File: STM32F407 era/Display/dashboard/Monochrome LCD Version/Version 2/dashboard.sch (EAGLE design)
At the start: 89 parts, among them IC2 74HC14D, IC3 74HC14D, U1 CAT4238TD-GT3

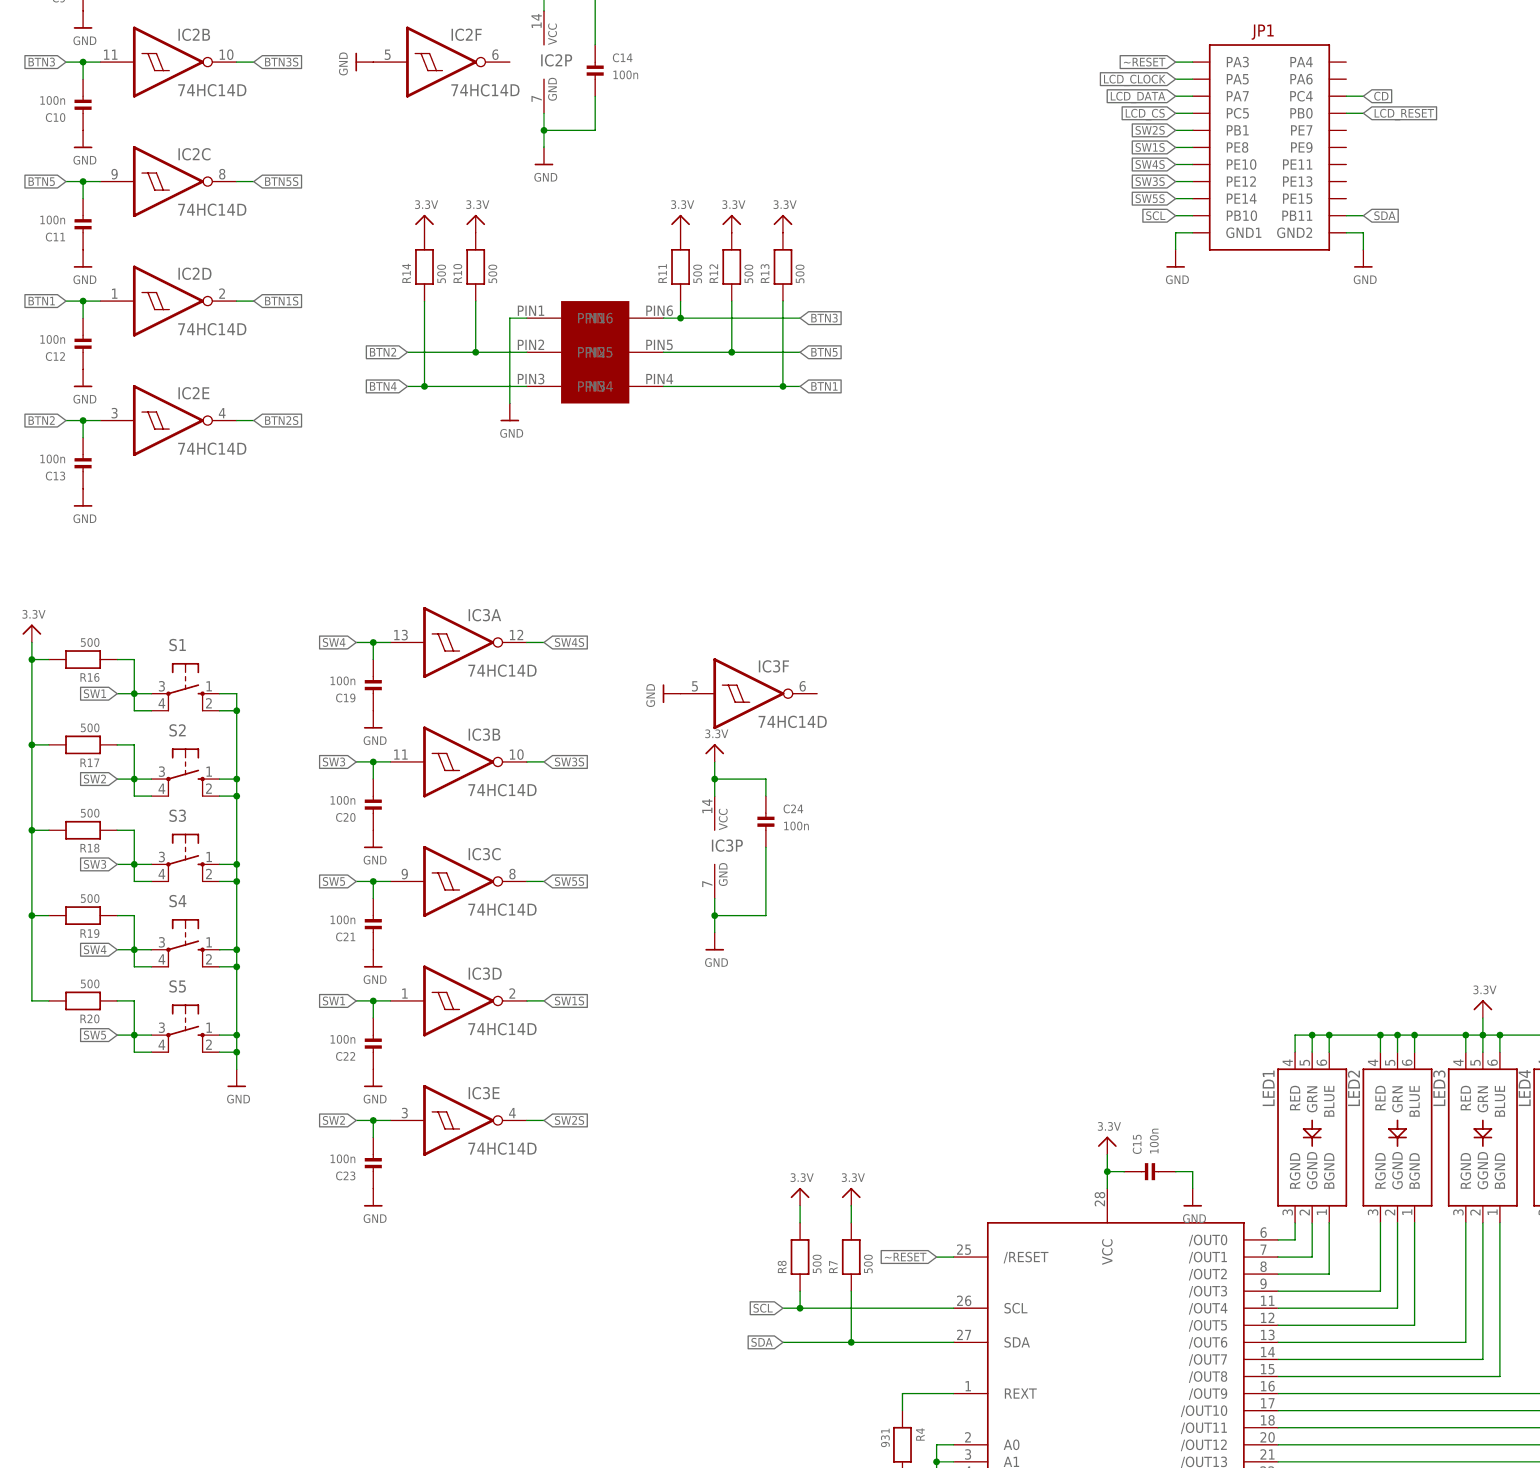
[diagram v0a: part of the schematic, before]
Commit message: fixed silkscreen and added extra button for interface
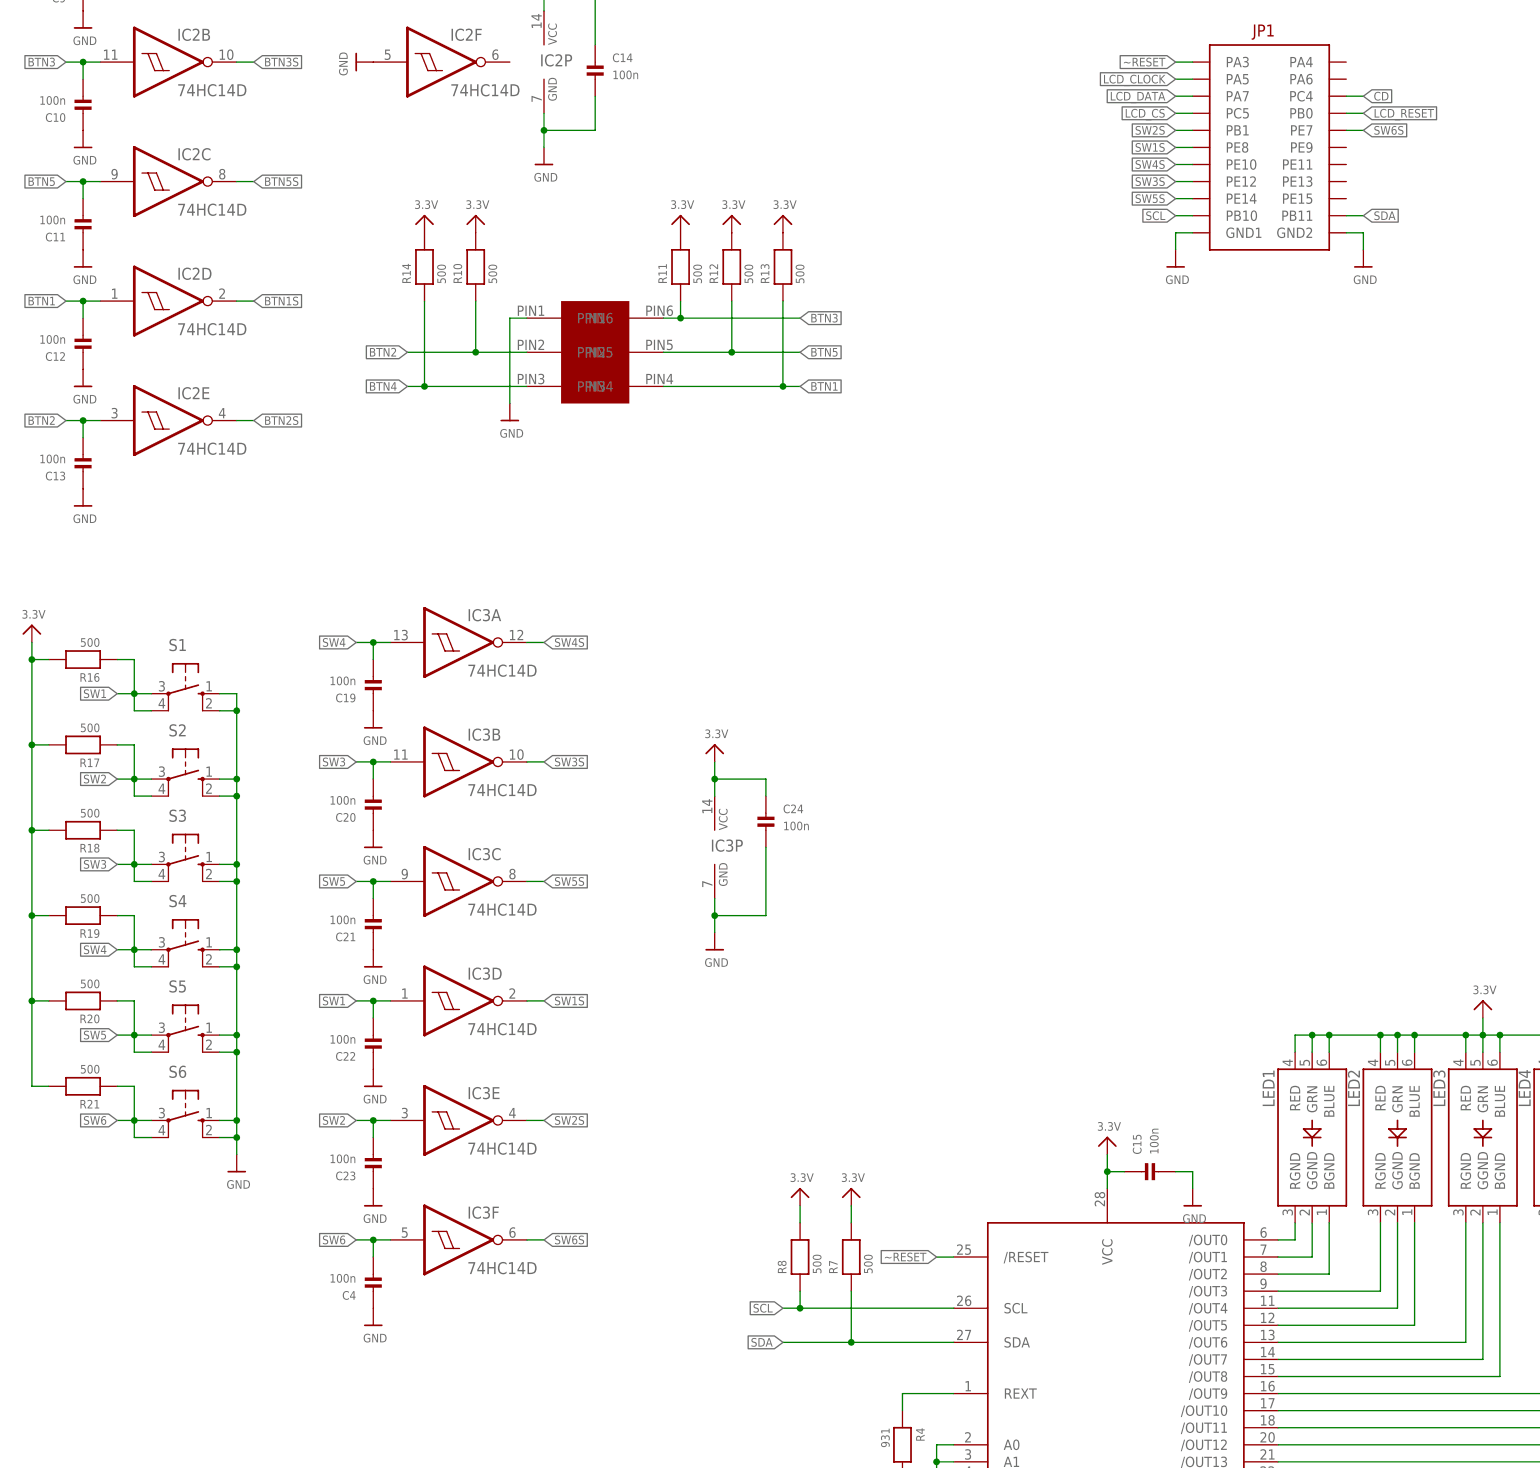
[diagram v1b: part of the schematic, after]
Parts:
- added C4: 100n, microbuilder:CAP_CERAMIC_0603
- added R21: 500, microbuilder:RESISTOR_0603
- added S6: (no value), switch-omron:10-XX
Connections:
- new net SW6: C4.P$2, IC3F.I, R21.1, S6.P, S6.P1
- new net SW6S: IC3F.O, U$1G$1.PE7
- net 3.3V: now also R21.2
- net GND: now also C4.P$1, S6.S, S6.S1; no longer IC3F.I
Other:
- moved on the sheet: IC3F
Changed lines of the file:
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@@
 <part name="U$71" library="microbuilder" deviceset="GND" device=""/>
 <part name="C24" library="microbuilder" deviceset="CAP_CERAMIC" device="_0603" value="100n"/>
-<part name="U$72" library="microbuilder" deviceset="GND" device=""/>
 <part name="U$73" library="microbuilder" deviceset="GND" device=""/>
 <part name="U$74" library="microbuilder" deviceset="3.3V" device=""/>
@@
 <part name="C25" library="rcl" deviceset="CPOL-EU" device="153CLV-1012" value="470u"/>
 <part name="C26" library="rcl" deviceset="CPOL-EU" device="153CLV-1012" value="220u"/>
+<part name="S6" library="switch-omron" deviceset="10-XX" device="">
+<attribute name="MF" value=""/>
+<attribute name="MPN" value="B3F-1000"/>
+<attribute name="OC_FARNELL" value="176432"/>
+<attribute name="OC_NEWARK" value="36M3542"/>
+</part>
+<part name="R21" library="microbuilder" deviceset="RESISTOR" device="_0603" value="500"/>
+<part name="C4" library="microbuilder" deviceset="CAP_CERAMIC" device="_0603" value="100n"/>
+<part name="U$72" library="microbuilder" deviceset="GND" device=""/>
 </parts>
 <sheets>
@@
 <instance part="S3" gate="1" x="-210.82" y="-55.88" rot="R270"/>
 <instance part="S4" gate="1" x="-210.82" y="-68.58" rot="R270"/>
-<instance part="U$53" gate="G$1" x="-203.2" y="-88.9"/>
+<instance part="U$53" gate="G$1" x="-203.2" y="-101.6"/>
 <instance part="R16" gate="G$1" x="-226.06" y="-25.4" rot="R180"/>
 <instance part="R17" gate="G$1" x="-226.06" y="-38.1" rot="R180"/>
@@
 <instance part="U$70" gate="G$1" x="-182.88" y="-88.9"/>
 <instance part="U$71" gate="G$1" x="-182.88" y="-106.68"/>
-<instance part="IC3" gate="F" x="-127" y="-30.48"/>
+<instance part="IC3" gate="F" x="-170.18" y="-111.76"/>
 <instance part="IC3" gate="P" x="-132.08" y="-53.34"/>
 <instance part="C24" gate="G$1" x="-124.46" y="-50.8"/>
-<instance part="U$72" gate="G$1" x="-139.7" y="-30.48" rot="R270"/>
 <instance part="U$73" gate="G$1" x="-132.08" y="-68.58"/>
 <instance part="U$74" gate="G$1" x="-132.08" y="-38.1"/>
@@
 <instance part="C25" gate="G$1" x="25.4" y="-53.34" rot="MR0"/>
 <instance part="C26" gate="G$1" x="83.82" y="-53.34" rot="MR0"/>
+<instance part="S6" gate="1" x="-210.82" y="-93.98" rot="R270"/>
+<instance part="R21" gate="G$1" x="-226.06" y="-88.9" rot="R180"/>
+<instance part="C4" gate="G$1" x="-182.88" y="-116.84" rot="R180"/>
+<instance part="U$72" gate="G$1" x="-182.88" y="-124.46"/>
 </instances>
 <busses>
@@
 <pinref part="S4" gate="1" pin="S"/>
 <wire x1="-203.2" y1="-81.28" x2="-203.2" y2="-83.82" width="0.1524" layer="91"/>
-<wire x1="-203.2" y1="-83.82" x2="-203.2" y2="-86.36" width="0.1524" layer="91"/>
+<wire x1="-203.2" y1="-83.82" x2="-203.2" y2="-93.98" width="0.1524" layer="91"/>
+<wire x1="-203.2" y1="-93.98" x2="-203.2" y2="-96.52" width="0.1524" layer="91"/>
+<wire x1="-203.2" y1="-96.52" x2="-203.2" y2="-99.06" width="0.1524" layer="91"/>
 <wire x1="-205.74" y1="-68.58" x2="-203.2" y2="-68.58" width="0.1524" layer="91"/>
 <wire x1="-203.2" y1="-68.58" x2="-203.2" y2="-71.12" width="0.1524" layer="91"/>
@@
 <wire x1="-205.74" y1="-81.28" x2="-203.2" y2="-81.28" width="0.1524" layer="91"/>
 <junction x="-203.2" y="-81.28"/>
+<pinref part="S6" gate="1" pin="S"/>
+<wire x1="-205.74" y1="-93.98" x2="-203.2" y2="-93.98" width="0.1524" layer="91"/>
+<junction x="-203.2" y="-93.98"/>
+<pinref part="S6" gate="1" pin="S1"/>
+<wire x1="-205.74" y1="-96.52" x2="-203.2" y2="-96.52" width="0.1524" layer="91"/>
+<junction x="-203.2" y="-96.52"/>
 </segment>
 <segment>
@@
 <pinref part="C23" gate="G$1" pin="P$1"/>
 <pinref part="U$71" gate="G$1" pin="GND"/>
-</segment>
-<segment>
-<pinref part="IC3" gate="F" pin="I"/>
-<pinref part="U$72" gate="G$1" pin="GND"/>
 </segment>
 <segment>
@@
 <wire x1="83.82" y1="-58.42" x2="83.82" y2="-63.5" width="0.1524" layer="91"/>
 <pinref part="C26" gate="G$1" pin="-"/>
+</segment>
+<segment>
+<pinref part="C4" gate="G$1" pin="P$1"/>
+<pinref part="U$72" gate="G$1" pin="GND"/>
 </segment>
 </net>
@@
 <wire x1="-233.68" y1="-76.2" x2="-233.68" y2="-63.5" width="0.1524" layer="91"/>
 <junction x="-233.68" y="-63.5"/>
+<pinref part="R21" gate="G$1" pin="2"/>
+<wire x1="-231.14" y1="-88.9" x2="-233.68" y2="-88.9" width="0.1524" layer="91"/>
+<wire x1="-233.68" y1="-88.9" x2="-233.68" y2="-76.2" width="0.1524" layer="91"/>
+<junction x="-233.68" y="-76.2"/>
 </segment>
 <segment>
@@
 </segment>
 </net>
+<net name="SW6" class="0">
+<segment>
+<pinref part="S6" gate="1" pin="P"/>
+<wire x1="-215.9" y1="-93.98" x2="-218.44" y2="-93.98" width="0.1524" layer="91"/>
+<wire x1="-218.44" y1="-93.98" x2="-218.44" y2="-88.9" width="0.1524" layer="91"/>
+<pinref part="R21" gate="G$1" pin="1"/>
+<wire x1="-218.44" y1="-88.9" x2="-220.98" y2="-88.9" width="0.1524" layer="91"/>
+<pinref part="S6" gate="1" pin="P1"/>
+<wire x1="-215.9" y1="-96.52" x2="-218.44" y2="-96.52" width="0.1524" layer="91"/>
+<wire x1="-218.44" y1="-96.52" x2="-218.44" y2="-93.98" width="0.1524" layer="91"/>
+<junction x="-218.44" y="-93.98"/>
+<wire x1="-220.98" y1="-93.98" x2="-218.44" y2="-93.98" width="0.1524" layer="91"/>
+<label x="-220.98" y="-93.98" size="1.27" layer="95" rot="R180" xref="yes"/>
+</segment>
+<segment>
+<pinref part="C4" gate="G$1" pin="P$2"/>
+<wire x1="-182.88" y1="-111.76" x2="-182.88" y2="-114.3" width="0.1524" layer="91"/>
+<wire x1="-185.42" y1="-111.76" x2="-182.88" y2="-111.76" width="0.1524" layer="91"/>
+<pinref part="IC3" gate="F" pin="I"/>
+<wire x1="-182.88" y1="-111.76" x2="-180.34" y2="-111.76" width="0.1524" layer="91"/>
+<junction x="-182.88" y="-111.76"/>
+<label x="-185.42" y="-111.76" size="1.27" layer="95" rot="R180" xref="yes"/>
+</segment>
+</net>
+<net name="SW6S" class="0">
+<segment>
+<pinref part="IC3" gate="F" pin="O"/>
+<wire x1="-157.48" y1="-111.76" x2="-160.02" y2="-111.76" width="0.1524" layer="91"/>
+<label x="-157.48" y="-111.76" size="1.27" layer="95" xref="yes"/>
+</segment>
+<segment>
+<pinref part="U$1" gate="G$1" pin="PE7"/>
+<wire x1="-35.56" y1="53.34" x2="-38.1" y2="53.34" width="0.1524" layer="91"/>
+<label x="-35.56" y="53.34" size="1.27" layer="95" xref="yes"/>
+</segment>
+</net>

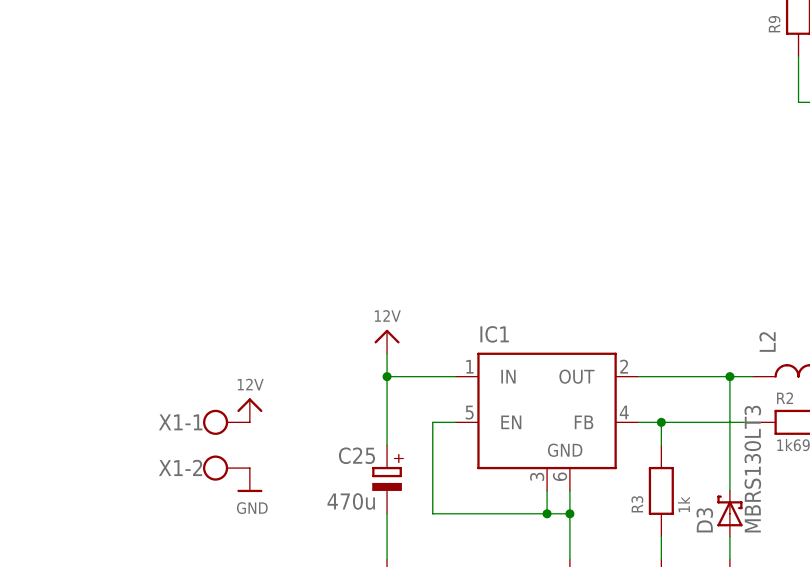
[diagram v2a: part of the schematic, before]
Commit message: adding last changes to accomendate changes in H-Bridge
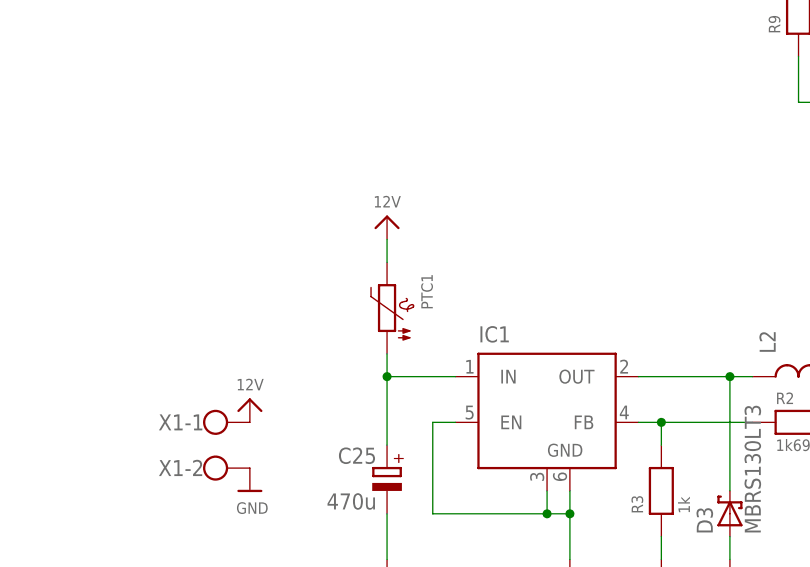
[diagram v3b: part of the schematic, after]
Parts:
- added PTC1: (no value), microbuilder:PTC1812
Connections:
- new net N$77: C25.+, IC1.IN, PTC1.1
- net 12V: now also PTC1.2; no longer C25.+, IC1.IN
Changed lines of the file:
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@@
 <part name="C4" library="microbuilder" deviceset="CAP_CERAMIC" device="_0603" value="100n"/>
 <part name="U$72" library="microbuilder" deviceset="GND" device=""/>
+<part name="PTC1" library="microbuilder" deviceset="PTC" device="1812"/>
 </parts>
 <sheets>
@@
 <instance part="R3" gate="G$1" x="55.88" y="-55.88" rot="R90"/>
 <instance part="U$19" gate="G$1" x="55.88" y="-66.04"/>
-<instance part="U$20" gate="G$1" x="25.4" y="-38.1"/>
+<instance part="U$20" gate="G$1" x="25.4" y="-25.4"/>
 <instance part="U$21" gate="G$1" x="25.4" y="-66.04"/>
 <instance part="U$22" gate="G$1" x="83.82" y="-66.04"/>
@@
 <instance part="C4" gate="G$1" x="-182.88" y="-116.84" rot="R180"/>
 <instance part="U$72" gate="G$1" x="-182.88" y="-124.46"/>
+<instance part="PTC1" gate="G$1" x="25.4" y="-35.56" rot="R270"/>
 </instances>
 <busses>
@@
 </segment>
 <segment>
-<pinref part="IC1" gate="G$1" pin="IN"/>
+<pinref part="PTC1" gate="G$1" pin="2"/>
 <pinref part="U$20" gate="G$1" pin="12V"/>
-<wire x1="33.02" y1="-43.18" x2="25.4" y2="-43.18" width="0.1524" layer="91"/>
-<wire x1="25.4" y1="-43.18" x2="25.4" y2="-40.64" width="0.1524" layer="91"/>
-<wire x1="25.4" y1="-43.18" x2="25.4" y2="-50.8" width="0.1524" layer="91"/>
-<junction x="25.4" y="-43.18"/>
-<pinref part="C25" gate="G$1" pin="+"/>
+<wire x1="25.4" y1="-30.48" x2="25.4" y2="-27.94" width="0.1524" layer="91"/>
 </segment>
 </net>
@@
 </segment>
 </net>
+<net name="N$77" class="0">
+<segment>
+<pinref part="IC1" gate="G$1" pin="IN"/>
+<wire x1="33.02" y1="-43.18" x2="25.4" y2="-43.18" width="0.1524" layer="91"/>
+<wire x1="25.4" y1="-43.18" x2="25.4" y2="-50.8" width="0.1524" layer="91"/>
+<pinref part="C25" gate="G$1" pin="+"/>
+<pinref part="PTC1" gate="G$1" pin="1"/>
+<wire x1="25.4" y1="-40.64" x2="25.4" y2="-43.18" width="0.1524" layer="91"/>
+<junction x="25.4" y="-43.18"/>
+</segment>
+</net>

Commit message: created Gerbers
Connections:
- net BTN1S: now also U$1G$2.PB13; no longer U$1G$2.PB12
- net BTN2S: now also U$1G$2.PB15; no longer U$1G$2.PB13
- net BTN3S: now also U$1G$2.PD11; no longer U$1G$2.PB14
- net BTN4S: now also U$1G$2.PC6; no longer U$1G$2.PD9
- net BTN5S: now also U$1G$2.PD9; no longer U$1G$2.PB15
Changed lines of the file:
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@@
 <net name="BTN1S" class="0">
-<segment>
-<pinref part="U$1" gate="G$2" pin="PB12"/>
-<wire x1="0" y1="63.5" x2="5.08" y2="63.5" width="0.1524" layer="91"/>
-<label x="0" y="63.5" size="1.27" layer="95" rot="R180" xref="yes"/>
-</segment>
 <segment>
 <pinref part="IC2" gate="D" pin="O"/>
@@
 <label x="-200.66" y="27.94" size="1.27" layer="95" xref="yes"/>
 </segment>
-</net>
-<net name="BTN2S" class="0">
 <segment>
 <pinref part="U$1" gate="G$2" pin="PB13"/>
@@
 <label x="33.02" y="63.5" size="1.27" layer="95" xref="yes"/>
 </segment>
+</net>
+<net name="BTN2S" class="0">
 <segment>
 <pinref part="IC2" gate="E" pin="O"/>
@@
 <label x="-200.66" y="10.16" size="1.27" layer="95" xref="yes"/>
 </segment>
+<segment>
+<pinref part="U$1" gate="G$2" pin="PB15"/>
+<wire x1="33.02" y1="60.96" x2="27.94" y2="60.96" width="0.1524" layer="91"/>
+<label x="33.02" y="60.96" size="1.27" layer="95" xref="yes"/>
+</segment>
 </net>
 <net name="BTN3S" class="0">
-<segment>
-<pinref part="U$1" gate="G$2" pin="PB14"/>
-<wire x1="0" y1="60.96" x2="5.08" y2="60.96" width="0.1524" layer="91"/>
-<label x="0" y="60.96" size="1.27" layer="95" rot="R180" xref="yes"/>
-</segment>
 <segment>
 <pinref part="IC2" gate="B" pin="O"/>
 <wire x1="-200.66" y1="63.5" x2="-203.2" y2="63.5" width="0.1524" layer="91"/>
 <label x="-200.66" y="63.5" size="1.27" layer="95" xref="yes"/>
+</segment>
+<segment>
+<pinref part="U$1" gate="G$2" pin="PD11"/>
+<wire x1="33.02" y1="55.88" x2="27.94" y2="55.88" width="0.1524" layer="91"/>
+<label x="33.02" y="55.88" size="1.27" layer="95" xref="yes"/>
 </segment>
 </net>
@@
 </segment>
 <segment>
-<pinref part="U$1" gate="G$2" pin="PD9"/>
-<wire x1="27.94" y1="58.42" x2="33.02" y2="58.42" width="0.1524" layer="91"/>
-<label x="33.02" y="58.42" size="1.27" layer="95" xref="yes"/>
+<pinref part="U$1" gate="G$2" pin="PC6"/>
+<wire x1="0" y1="48.26" x2="5.08" y2="48.26" width="0.1524" layer="91"/>
+<label x="0" y="48.26" size="1.27" layer="95" rot="R180" xref="yes"/>
 </segment>
 </net>
@@
 </segment>
 <segment>
-<pinref part="U$1" gate="G$2" pin="PB15"/>
-<wire x1="33.02" y1="60.96" x2="27.94" y2="60.96" width="0.1524" layer="91"/>
-<label x="33.02" y="60.96" size="1.27" layer="95" xref="yes"/>
+<pinref part="U$1" gate="G$2" pin="PD9"/>
+<wire x1="27.94" y1="58.42" x2="33.02" y2="58.42" width="0.1524" layer="91"/>
+<label x="33.02" y="58.42" size="1.27" layer="95" xref="yes"/>
 </segment>
 </net>
